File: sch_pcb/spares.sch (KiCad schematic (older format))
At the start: 88 parts, among them J301 SPARE, J302 SPARE, J303 SPARE, J304 SPARE, J305 USER_GPIO_2, J306 SPARE, J307 SPARE, J308 USER_GPIO_1, J309 SPARE, J310 SPARE, J311 USER_ADC, J313 SPARE, J314 SPARE, J315 12VDC_IN, Q301 SPARE, Q302 SPARE, U106 MCP4351, U301 MCP23017, U302 SPARE, U303 SPARE, U304 MCP3008, U305 MCP1703A-2502/MB, U306 TPS54302

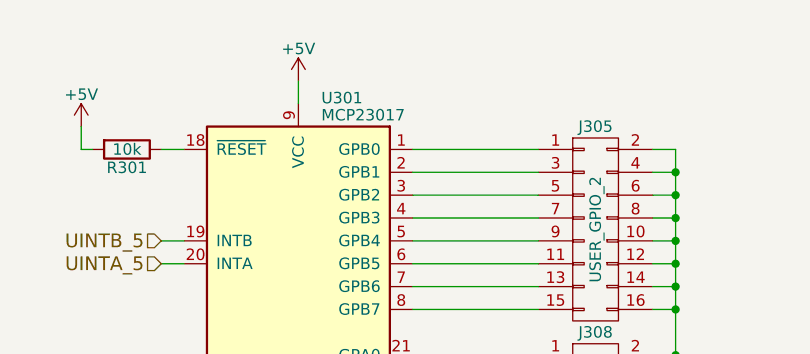
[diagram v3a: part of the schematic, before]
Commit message: Add files via upload
Reversed ends on all pots so up increases level
Added outline and mounting holes to RasPi footprint so we can see how big it really is
Moved parts away from one of the RasPi mounting holes so we can use all 4 of them
More routing - finished user GPIO and ADC, SPI chipselect decoder
Still to do: level shifters, RasPi connections and spares
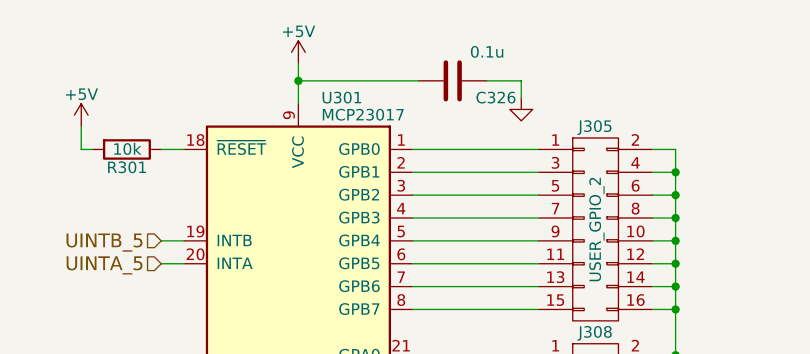
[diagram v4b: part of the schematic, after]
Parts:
- added C326: 0.1u, lib:smd0603, symbol C
- L301: footprint (none) -> lib:Inductor_Wurth_7447714100
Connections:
- net +5V: now also C326.2
- net GND: now also C326.1
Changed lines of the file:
@@
 L +5V #PWR0107
 U 1 1 596B3599
-P 7775 750
-F 0 "#PWR0107" H 7775 600 50  0001 C CNN
-F 1 "+5V" H 7775 890 50  0000 C CNN
-F 2 "" H 7775 750 50  0001 C CNN
-F 3 "" H 7775 750 50  0001 C CNN
-	1    7775 750
+P 7775 675
+F 0 "#PWR0107" H 7775 525 50  0001 C CNN
+F 1 "+5V" H 7775 815 50  0000 C CNN
+F 2 "" H 7775 675 50  0001 C CNN
+F 3 "" H 7775 675 50  0001 C CNN
+	1    7775 675
 	1    0    0    -1
 $EndComp
@@
 F 0 "L301" V 2775 6875 50  0000 C CNN
 F 1 "10uH" V 2935 6875 50  0000 C CNN
-F 2 "" H 2825 6875 50  0001 C CNN
+F 2 "lib:Inductor_Wurth_7447714100" H 2825 6875 50  0001 C CNN
 F 3 "" H 2825 6875 50  0001 C CNN
 	1    2825 6875
@@
 Connection ~ 7225 2650
 Wire Wire Line
-	7775 850  7775 750
+	7775 850  7775 675
 Wire Wire Line
 	7275 1050 7175 1050
@@
 	9325 2650 9425 2650
 Connection ~ 9425 2650
+$Comp
+L C C326
+U 1 1 59626760
+P 8450 750
+F 0 "C326" V 8525 850 50  0000 L CNN
+F 1 "0.1u" V 8325 825 50  0000 L CNN
+F 2 "lib:smd0603" H 8488 600 50  0001 C CNN
+F 3 "" H 8450 750 50  0001 C CNN
+	1    8450 750
+	0    1    1    0
+$EndComp
+Wire Wire Line
+	8300 750  7775 750
+Connection ~ 7775 750
+Wire Wire Line
+	8600 750  8750 750
+Wire Wire Line
+	8750 750  8750 825
+$Comp
+L GND #PWR0145
+U 1 1 59628314
+P 8750 825
+F 0 "#PWR0145" H 8750 575 50  0001 C CNN
+F 1 "GND" H 8750 675 50  0001 C CNN
+F 2 "" H 8750 825 50  0001 C CNN
+F 3 "" H 8750 825 50  0001 C CNN
+	1    8750 825
+	1    0    0    -1
+$EndComp
 $EndSCHEMATC

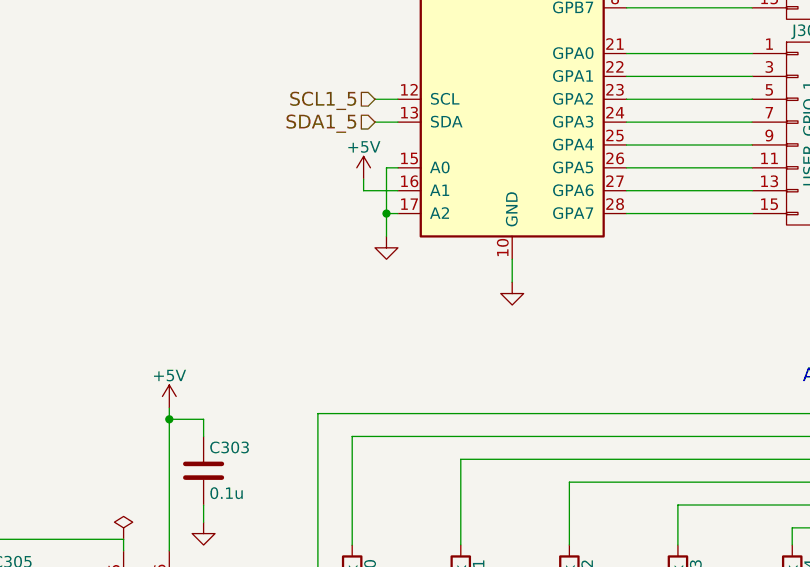
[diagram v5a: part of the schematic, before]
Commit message: Add soundcard schematic
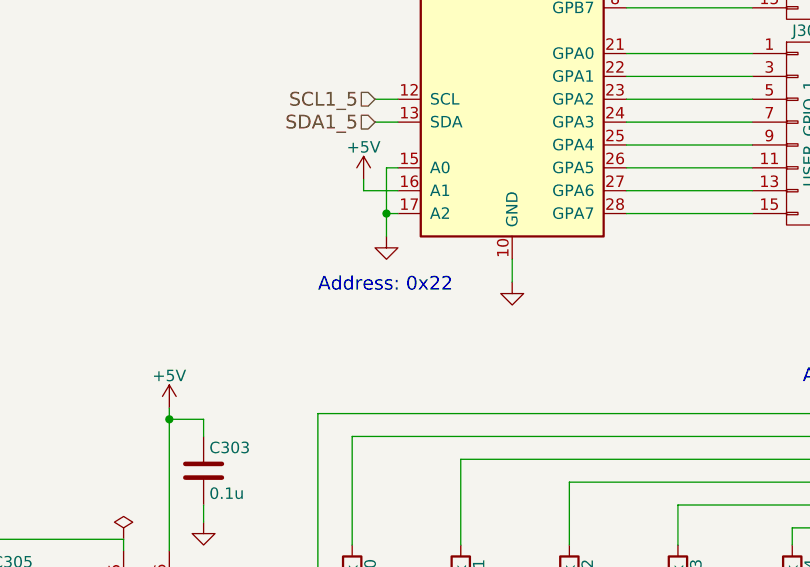
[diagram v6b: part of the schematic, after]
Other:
- note added: "Address: 0x22"

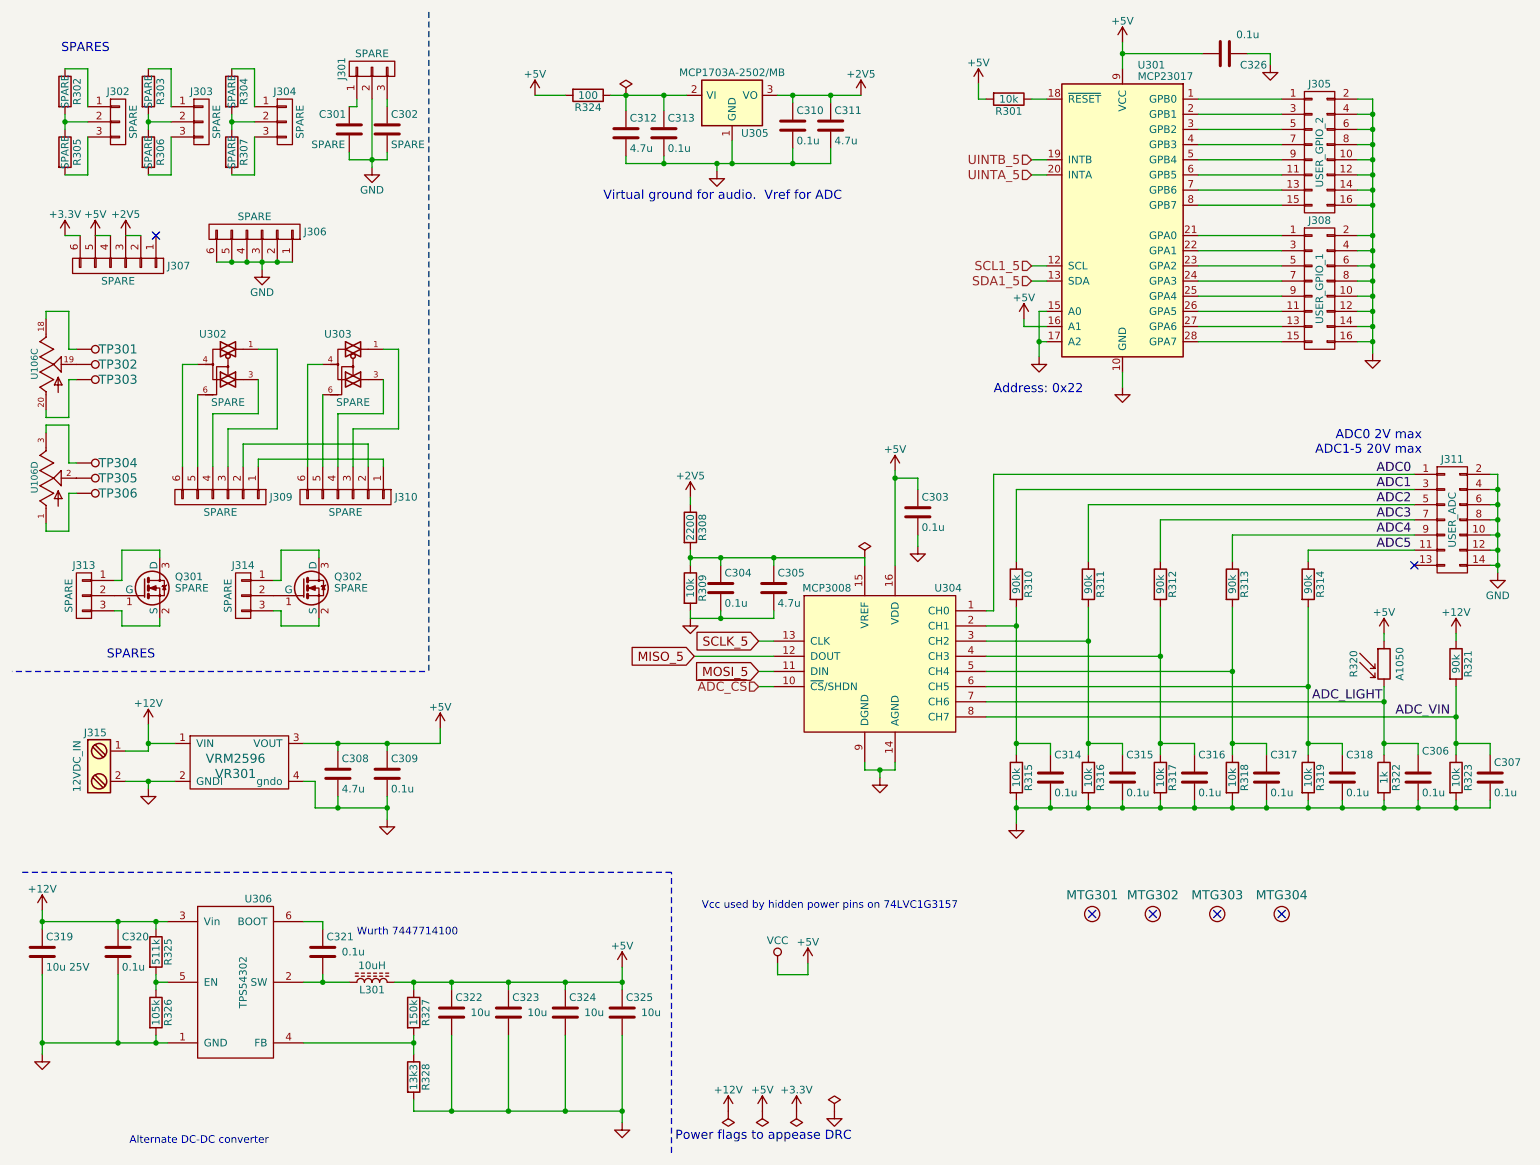
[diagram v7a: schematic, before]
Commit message: Update from latest round of emails
Change connectors - use correct footprint for DE9F.  Add chassis connector as DE9M, AUX_IO connectors as 116-pin ribbon, expected to transition to DA15 with a cable.  
Remove screw terminals for 12V input as it now comes in on chassis connector
Remove third EEPOT package
Move stuff off PCB in preparation to incorporate all the schematic updates.
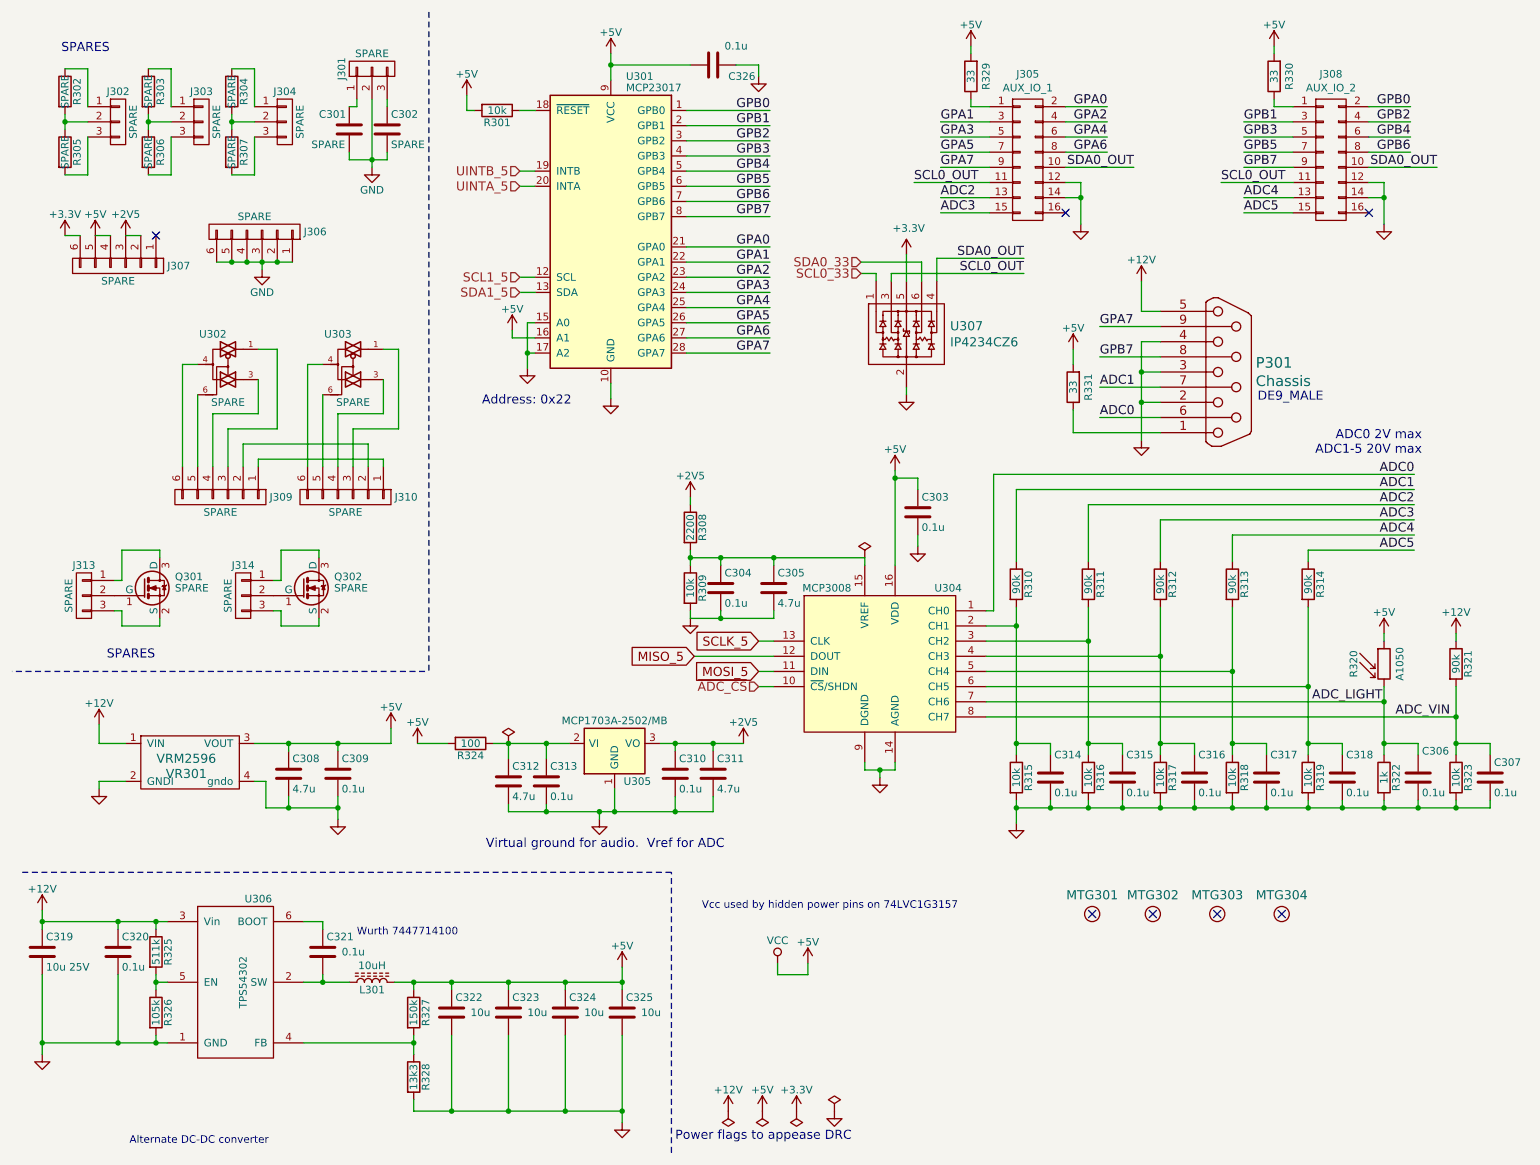
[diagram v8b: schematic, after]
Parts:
- removed J311: USER_ADC, lib:RibbonHeader2x7, symbol CONN_02X07
- removed J315: 12VDC_IN, ardai:Phoenix_2pin_3.5mm_conn_1984963, symbol Screw_Terminal_1x02
- removed TP301, TP302, TP303, TP304, TP305, TP306: TESTPOINT, lib:Wire_28AWG, symbol TESTPOINT
- removed U106: MCP4351, lib:SSOP-20, symbol MCP344XD
- added P301: Chassis, lib:DE9M_Right_Angle, symbol DE9
- added R329, R330, R331: 33, lib:smd0603, symbol R
- added U307: IP4234CZ6, lib:SOT23-6, symbol IP4234CZ6_USB_ESD_PROTECTOR
- J305: value USER_GPIO_2 -> AUX_IO_1
- J308: value USER_GPIO_1 -> AUX_IO_2
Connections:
- net +12V: now also P301.5
- net +3V3: now also U307.5
- net +5V: now also R329.2, R330.2, R331.2
- net ADC0: now also P301.6 (P6)
- net ADC1: now also P301.7 (P7)
- net ADC2: now also J305.13 (P13)
- net ADC3: now also J305.15 (P15)
- net ADC4: now also J308.13 (P13)
- net ADC5: now also J308.15 (P15)
- net GND: now also P301.2, P301.3, P301.4, U307.2; no longer J305.10 (P10), J305.16 (P16), J305.2 (P2), J305.4 (P4), J305.6 (P6), J305.8 (P8), J308.10 (P10), J308.16 (P16), J308.2 (P2), J308.4 (P4), J308.6 (P6), J308.8 (P8)
- net at J305.1 (P1): now also R329.1; no longer U301.1 (GPB0)
- net GPB5: now reaches U301.6 (GPB5)
- net GPB5: now also J308.7 (P7); no longer J305.11 (P11)
- net GPB6: now reaches U301.7 (GPB6)
- net GPB6: now also J308.8 (P8); no longer J305.13 (P13)
- net GPB7: now reaches U301.8 (GPB7)
- net GPB7: now also J308.9 (P9), P301.8 (P8); no longer J305.15 (P15)
- net GPA1: now reaches J305.3 (P3)
- net GPA1: now also U301.22 (GPA1); no longer U301.2 (GPB1)
- net GPA3: now reaches J305.5 (P5)
- net GPA3: now also U301.24 (GPA3); no longer U301.3 (GPB2)
- net GPA5: now reaches J305.7 (P7)
- net GPA5: now also U301.26 (GPA5); no longer U301.4 (GPB3)
- net GPA7: now reaches J305.9 (P9)
- net GPA7: now also U301.28 (GPA7), P301.9 (P9); no longer U301.5 (GPB4)
- net at J308.1 (P1): now also R330.1; no longer U301.21 (GPA0)
- net SCL0_OUT: now reaches J308.11 (P11)
- net SCL0_OUT: now also J305.11 (P11), U307.3; no longer U301.26 (GPA5)
- net GPA6: now reaches U301.27 (GPA6)
- net GPA6: now also J305.8 (P8); no longer J308.13 (P13)
- net GPB1: now reaches J308.3 (P3)
- net GPB1: now also U301.2 (GPB1); no longer U301.22 (GPA1)
- net GPA2: now reaches U301.23 (GPA2)
- net GPA2: now also J305.4 (P4); no longer J308.5 (P5)
- net GPA4: now reaches U301.25 (GPA4)
- net GPA4: now also J305.6 (P6); no longer J308.9 (P9)
- new net: P301.1, R331.1
- new net GPA0: J305.2 (P2), U301.21 (GPA0)
- new net GPB0: J308.2 (P2), U301.1 (GPB0)
- new net GPB2: J308.4 (P4), U301.3 (GPB2)
- new net GPB3: J308.5 (P5), U301.4 (GPB3)
- new net GPB4: J308.6 (P6), U301.5 (GPB4)
- new net SCL0_33: U307.1
- new net SDA0_33: U307.6
- new net SDA0_OUT: J305.10 (P10), J308.10 (P10), U307.4
- no-connect marks 6 -> 7
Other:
- note added: "DE9_MALE"
- moved on the sheet: C308, C309, C310, C311, C312, C313, C326, R301, R324, U301, U305, VR301
